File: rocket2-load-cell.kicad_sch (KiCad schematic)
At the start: 38 parts, among them J1 SWD, J2 Screw_Terminal_01x02, U2 STM32F103C8Tx, U3 AMS1117-3.3, Y1 16MHz

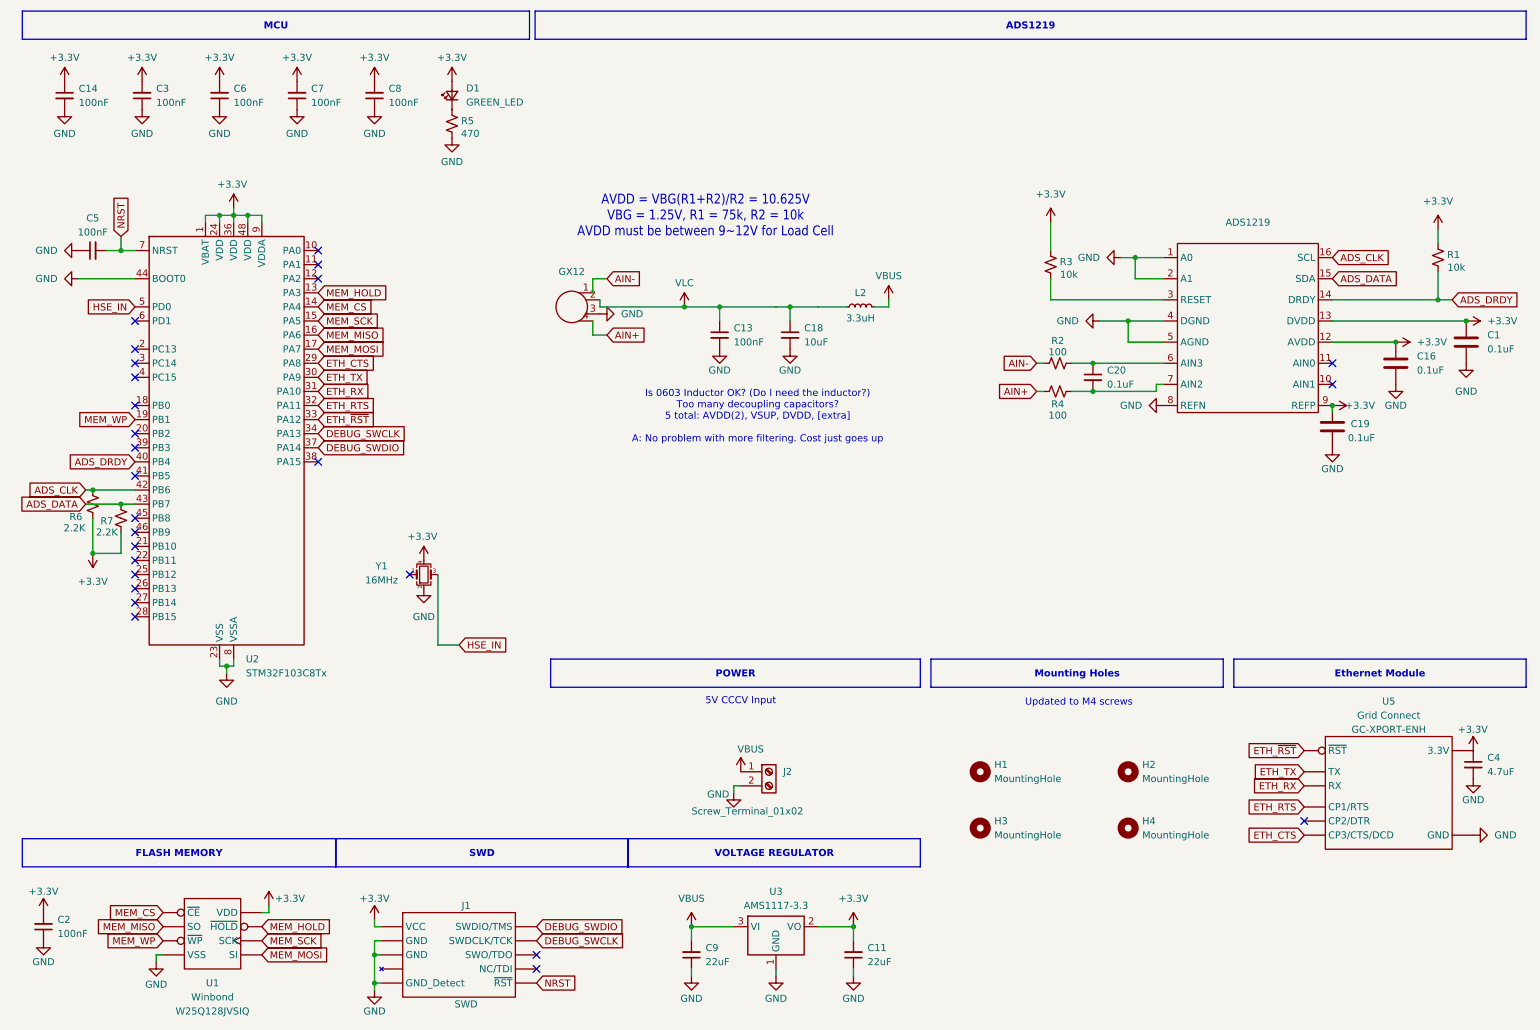
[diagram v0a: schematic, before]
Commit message: Minor Schematic Fixes
>> TX and RX lines now connected to their respective opposites (e.g. TX -> RX)
>> Changed connector to new standard based on the new load cell
>> Added datasheets to all schematic symbols
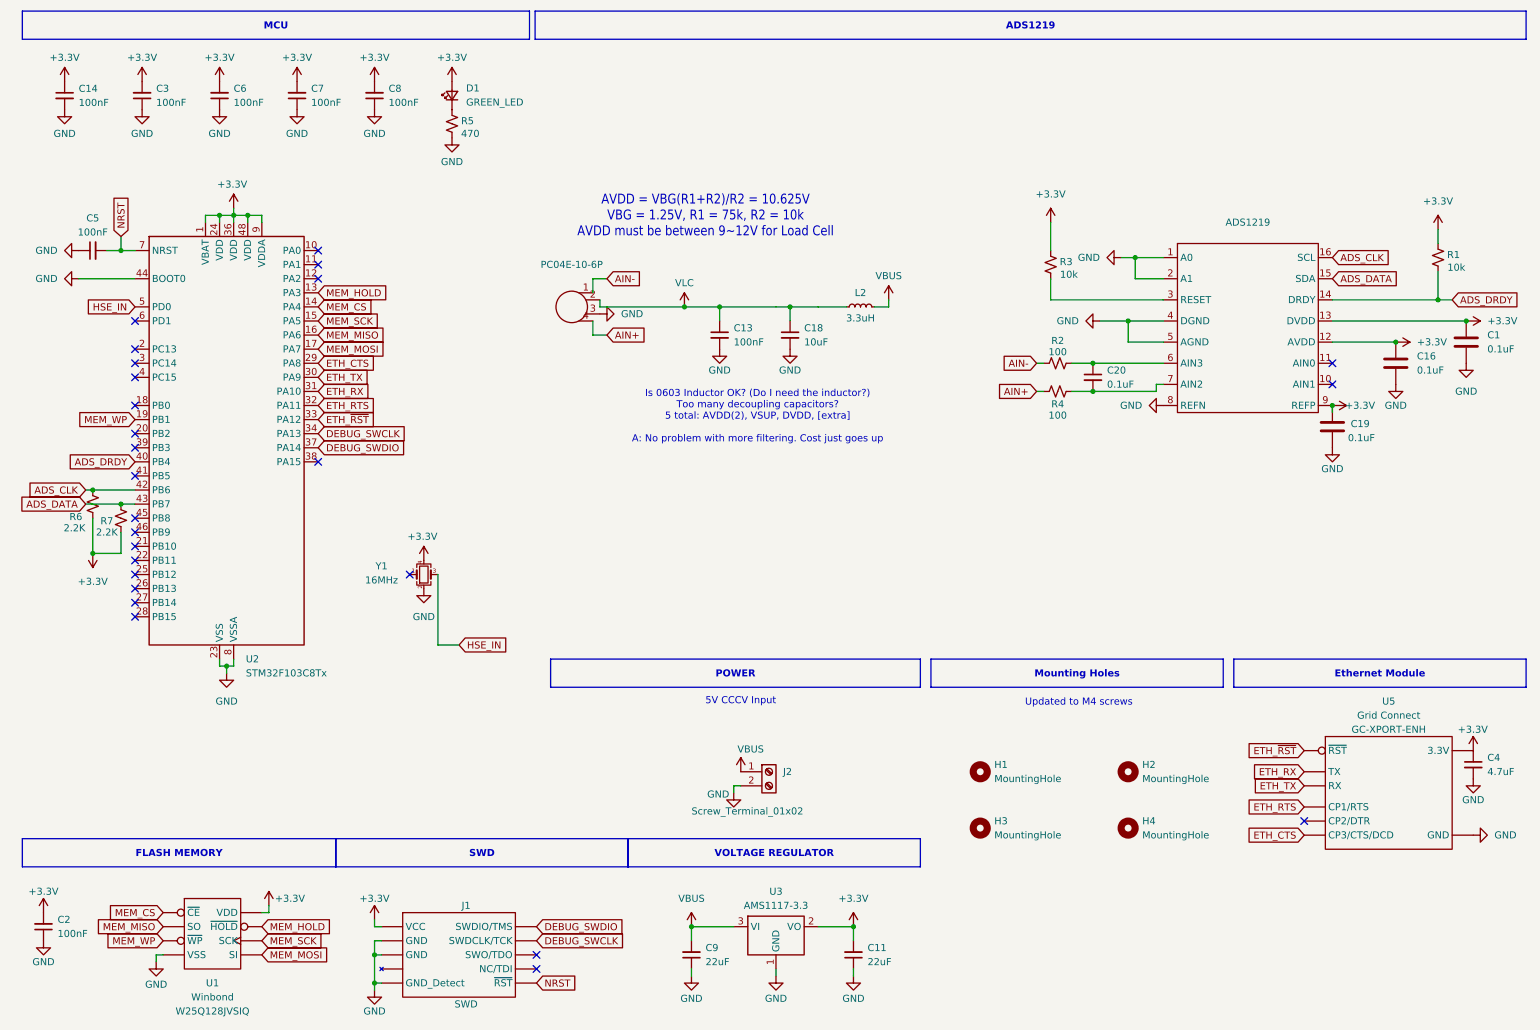
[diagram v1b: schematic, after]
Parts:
- renumbered GX12 to PC04E-10-6P
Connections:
- net ETH_RX: now also U5.4 (TX); no longer U5.5 (RX)
- net ETH_TX: now also U5.5 (RX); no longer U5.4 (TX)

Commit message: Added USB-B and Filtering
Replaced memory w/ USB-B connector and strengthened passive RC filtering for differential analog inputs to ADC.
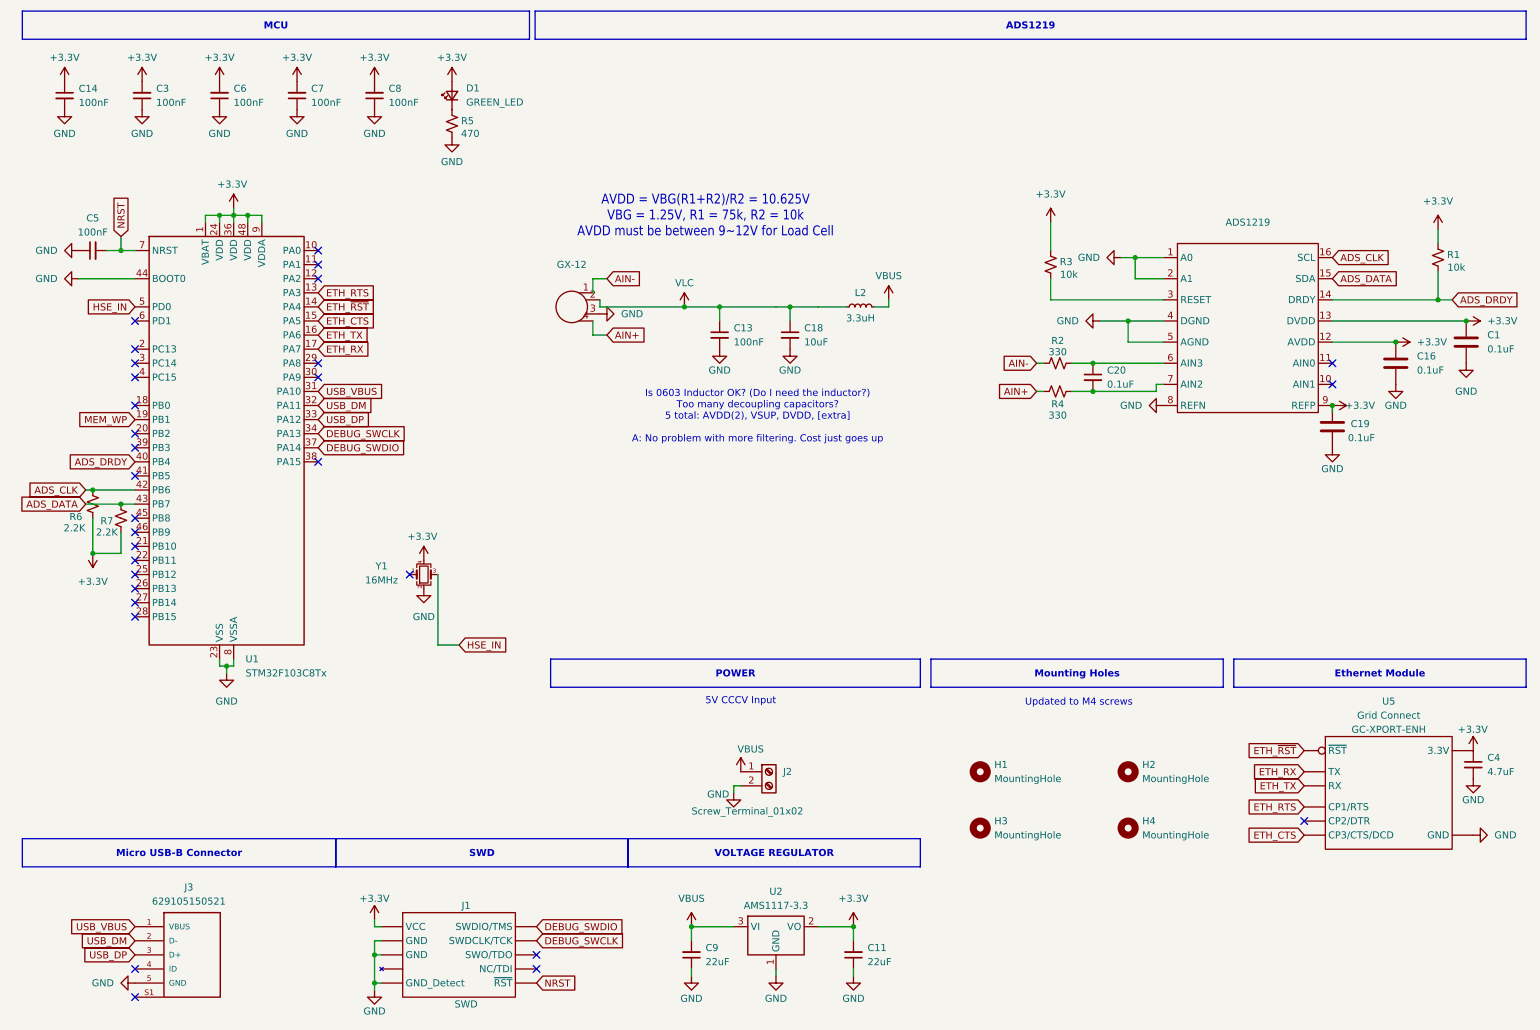
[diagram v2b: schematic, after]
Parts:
- removed C2: 100nF, Capacitor_SMD:C_0603_1608Metric, symbol Device:C_Small
- removed U1: ~, Package_SO:SOIC-8W_5.3x5.3mm_P1.27mm, symbol UCIRP-KiCAD-Lib:SST25VF016B
- added J3: 629105150521, symbol UCIRP-KiCAD-Lib:629105150521
- R2, R4: value 100 -> 330
- renumbered PC04E-10-6P to GX-12, U2 to U1, U3 to U2
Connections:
- net MEM_CS is gone; now on net ETH_~{RST}: U1.14 (PA4)
- net MEM_HOLD is gone; now on net ETH_RTS: U1.13 (PA3)
- net MEM_MISO is gone; now on net ETH_TX: U1.16 (PA6)
- net MEM_MOSI is gone; now on net ETH_RX: U1.17 (PA7)
- net MEM_SCK is gone; now on net ETH_CTS: U1.15 (PA5)
- net ETH_CTS: no longer U1.29 (PA8)
- net ETH_RTS: no longer U1.32 (PA11)
- net ETH_RX: no longer U1.31 (PA10)
- net ETH_TX: no longer U1.30 (PA9)
- net ETH_~{RST}: no longer U1.33 (PA12)
- net GND: now also J3.5 (GND)
- new net USB_DM: J3.2 (D-), U1.32 (PA11)
- new net USB_DP: J3.3 (D+), U1.33 (PA12)
- new net USB_VBUS: J3.1 (VBUS), U1.31 (PA10)
- no-connect marks 26 -> 30

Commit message: PCB Updates + Schematic Adjustments
Layout, signal lines, and basis for power routing.

Added a voltage divider to the USB_VBUS pin to protect GPIO.
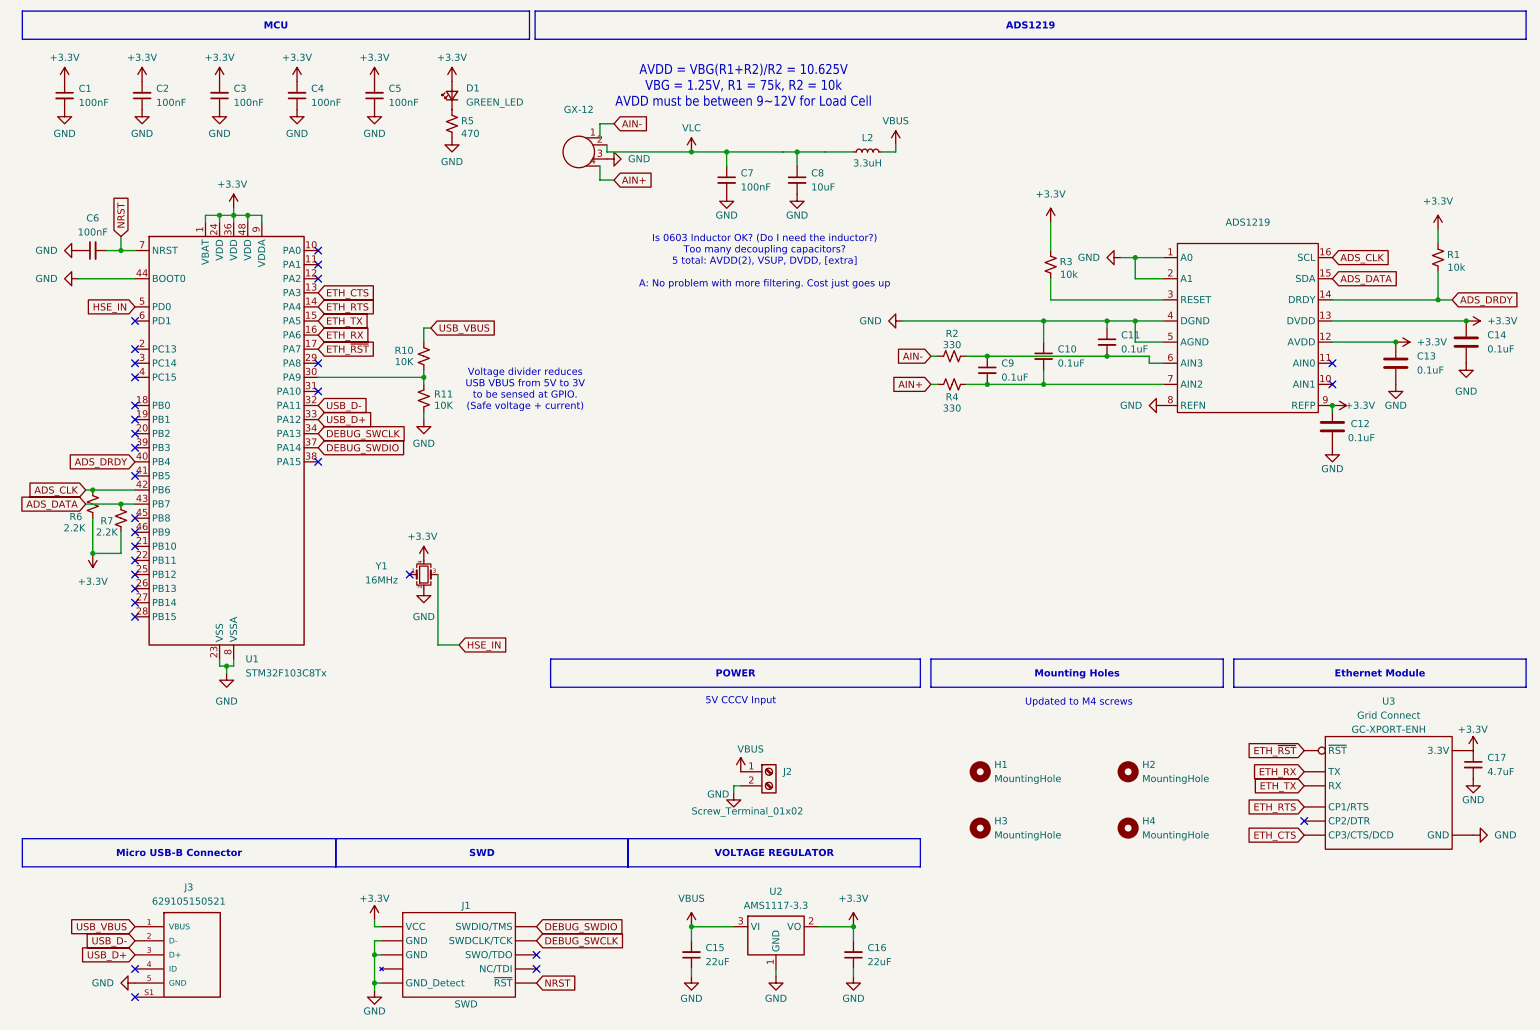
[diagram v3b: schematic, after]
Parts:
- added C10, C11: 0.1uF, Capacitor_SMD:C_0603_1608Metric, symbol Device:C_Small
- added R10, R11: 10K, Resistor_SMD:R_0603_1608Metric, symbol Device:R_Small_US
- J3: footprint (none) -> Connector_USB:USB_Micro-B_Wuerth_629105150521
- U3: renamed from U5; footprint GSE:GC-XPORT -> UCIRP-KiCAD-Lib:GC-XPORT
- renumbered C14 to C1, C19 to C12, C16 to C13, C1 to C14, C9 to C15, C11 to C16, C4 to C17, C3 to C2, C6 to C3, C7 to C4, C8 to C5, C5 to C6, C13 to C7, C18 to C8, C20 to C9
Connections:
- net ETH_CTS: now also U1.13 (PA3); no longer U1.15 (PA5)
- net ETH_RTS: now also U1.14 (PA4); no longer U1.13 (PA3)
- net ETH_RX: now also U1.16 (PA6); no longer U1.17 (PA7)
- net ETH_TX: now also U1.15 (PA5); no longer U1.16 (PA6)
- net ETH_~{RST}: now also U1.17 (PA7); no longer U1.14 (PA4)
- net GND: now also C10.1, C11.1, R11.1
- net USB_VBUS: now also R10.2; no longer U1.31 (PA10)
- net at U1.30 (PA9): now also R10.1, R11.2
- net at ADS1219.7 (AIN2), C9.2, R4.2: now also C10.2
- net at ADS1219.6 (AIN3), C9.1, R2.2: now also C11.2
- net MEM_WP: no longer names the net of U1.19 (PB1)
- net USB_DM renamed USB_D-
- net USB_DP renamed USB_D+
- no-connect marks 30 -> 31
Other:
- note added: "Voltage divider reduces USB VBUS from 5V to 3V to be sensed at GPIO. (Safe voltage + current)"
- moved on the sheet: C7, C8, C9, GX-12, L2, R2, R4

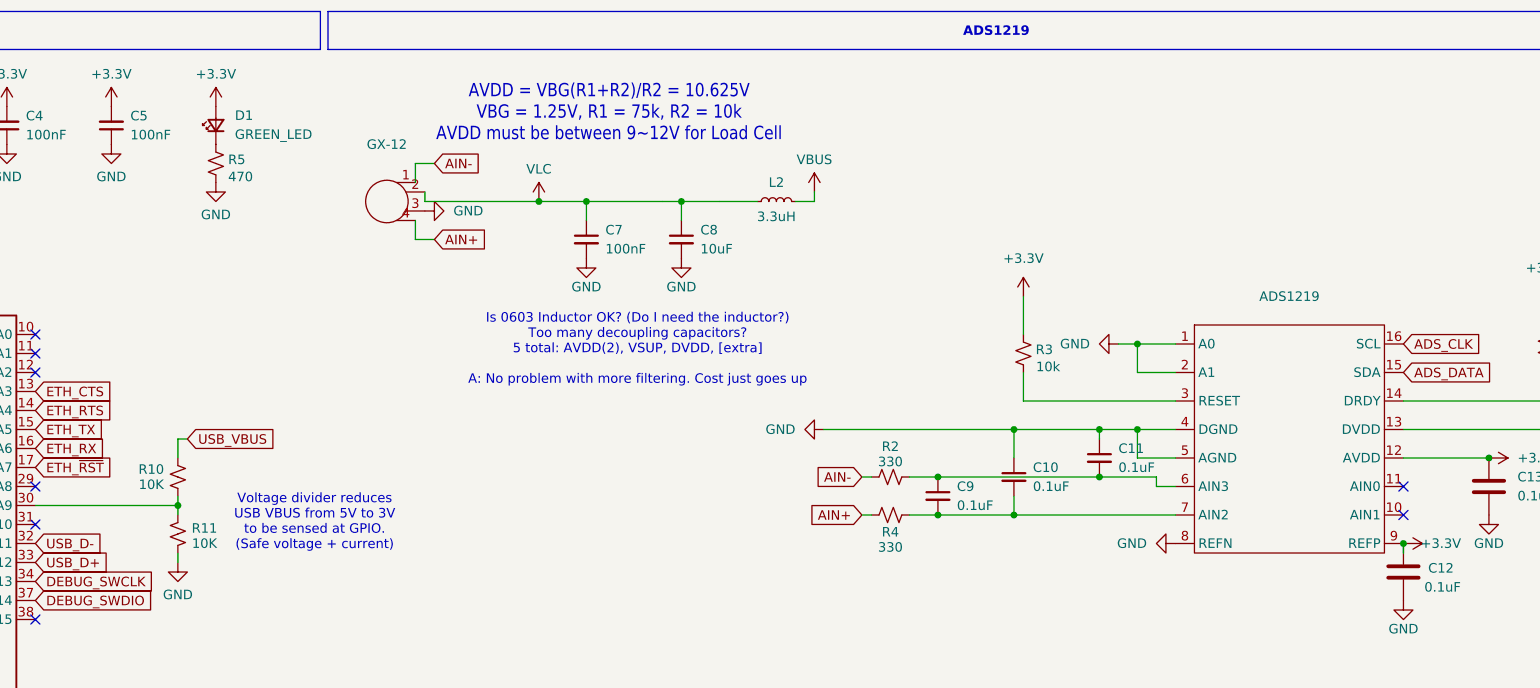
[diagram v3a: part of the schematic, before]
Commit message: complete power + signal routing
fixed bends, shortened length from MCU -> ADC -> Load Cell
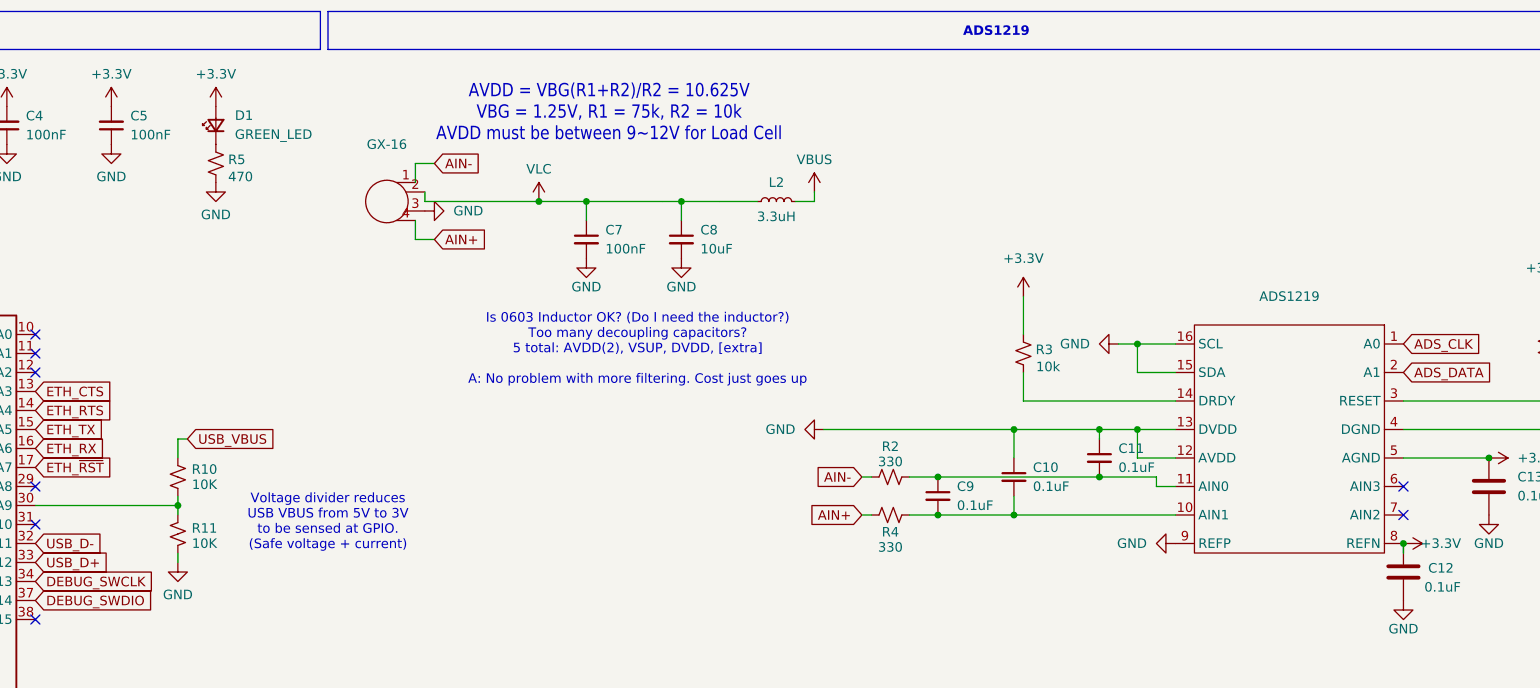
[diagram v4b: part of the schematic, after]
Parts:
- GX-16: renamed from GX-12; footprint UCIRP-KiCAD-Lib:gx12 -> UCIRP-KiCAD-Lib:GX16-4
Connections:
- net +3.3V: now also ADS1219.4 (DGND), ADS1219.5 (AGND), ADS1219.8 (REFN); no longer ADS1219.12 (AVDD), ADS1219.13 (DVDD), ADS1219.9 (REFP)
- net ADS_CLK: now also ADS1219.1 (A0); no longer ADS1219.16 (SCL)
- net ADS_DATA: now also ADS1219.2 (A1); no longer ADS1219.15 (SDA)
- net ADS_DRDY: now also ADS1219.3 (RESET); no longer ADS1219.14 (DRDY)
- net GND: now also ADS1219.12 (AVDD), ADS1219.13 (DVDD), ADS1219.15 (SDA), ADS1219.16 (SCL), ADS1219.9 (REFP); no longer ADS1219.1 (A0), ADS1219.2 (A1), ADS1219.4 (DGND), ADS1219.5 (AGND), ADS1219.8 (REFN)
- net at C11.2, C9.1, R2.2: now also ADS1219.11 (AIN0); no longer ADS1219.6 (AIN3)
- net at C10.2, C9.2, R4.2: now also ADS1219.10 (AIN1); no longer ADS1219.7 (AIN2)
- net at R3.1: now also ADS1219.14 (DRDY); no longer ADS1219.3 (RESET)
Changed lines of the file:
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@@
 	(text "Voltage divider reduces \nUSB VBUS from 5V to 3V \nto be sensed at GPIO.\n(Safe voltage + current)\n"
 		(exclude_from_sim no)
-		(at 103.378 81.026 0)
+		(at 105.156 81.026 0)
 		(effects
 			(font
@@
 		(on_board yes)
 		(dnp no)
-		(property "Reference" "GX-12"
+		(property "Reference" "GX-16"
 			(at 113.03 30.48 0)
 			(effects
@@
 			)
 		)
-		(property "Footprint" "UCIRP-KiCAD-Lib:gx12"
+		(property "Footprint" "UCIRP-KiCAD-Lib:GX16-4"
 			(at 113.03 38.1 0)
 			(effects
@@
 			(project "rocket2-load-cell"
 				(path "/d1f04dc8-a56c-4379-8ad0-2916e7244fc3"
-					(reference "GX-12")
+					(reference "GX-16")
 					(unit 1)
 				)
@@
 		(lib_id "load-cell-lib:ADS1219")
 		(at 233.68 69.85 0)
+		(mirror y)
 		(unit 1)
 		(exclude_from_sim no)
@@
 		(on_board yes)
 		(dnp no)
-		(fields_autoplaced yes)
 		(property "Reference" "ADS1219"
 			(at 233.68 50.8 0)
@@
 		(dnp no)
 		(property "Reference" "R10"
-			(at 81.534 73.914 0)
+			(at 88.646 73.914 0)
 			(effects
 				(font
@@
 		)
 		(property "Value" "10K"
-			(at 81.534 75.946 0)
+			(at 88.646 75.946 0)
 			(effects
 				(font
